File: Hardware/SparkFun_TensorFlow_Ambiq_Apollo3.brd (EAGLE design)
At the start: 40 x 40 mm, 122 parts, among them J5 CORTEX_DEBUG_PTH, J6 CAMERA-0V7670, M1 MEMS_MICROPHONESPW2430HR5H-B, M2 MEMS_MICROPHONESPW2430HR5H-B, U1 AMBIQ-APOLLO3KBR, U2 LIS2DH12, U3 1.8V, U4 LMV358, Y1 32MHz, Y2 32.768kHz

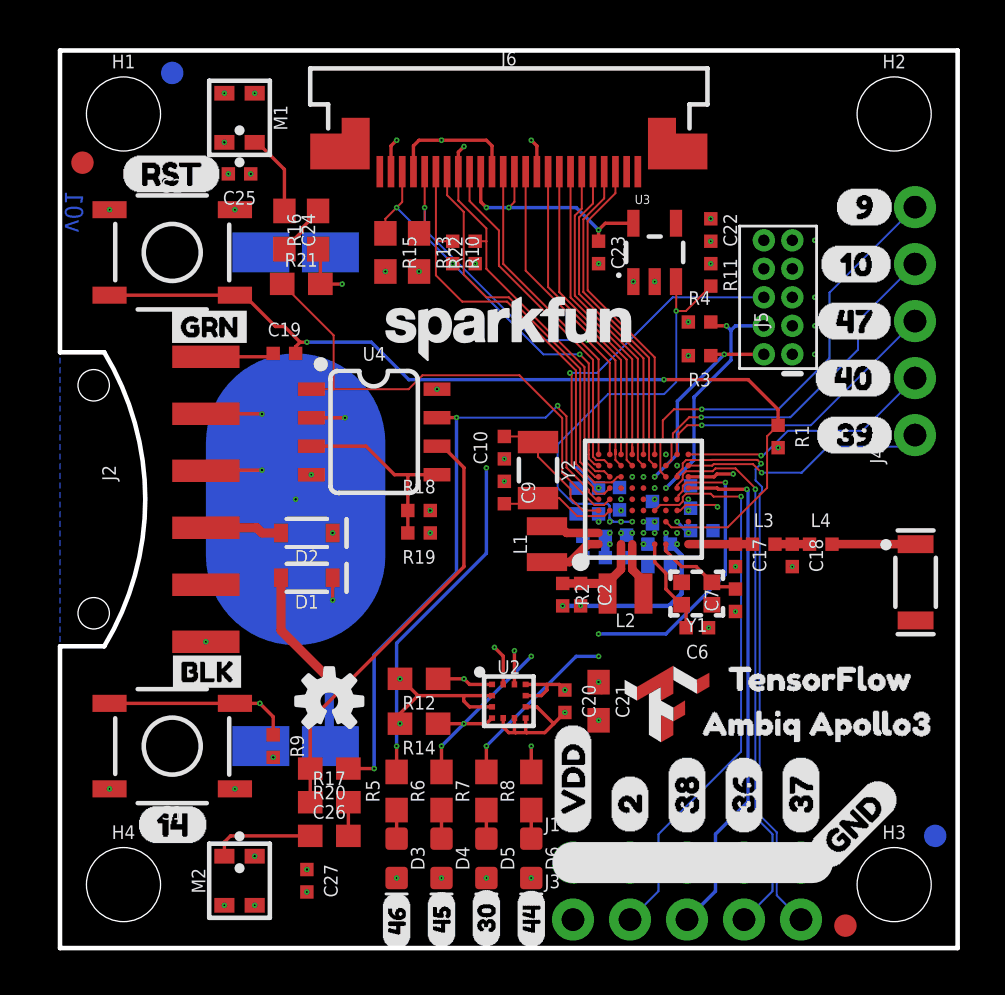
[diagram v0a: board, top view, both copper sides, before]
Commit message: Setting trace width/clearance to 5mil, via size to .2mm min
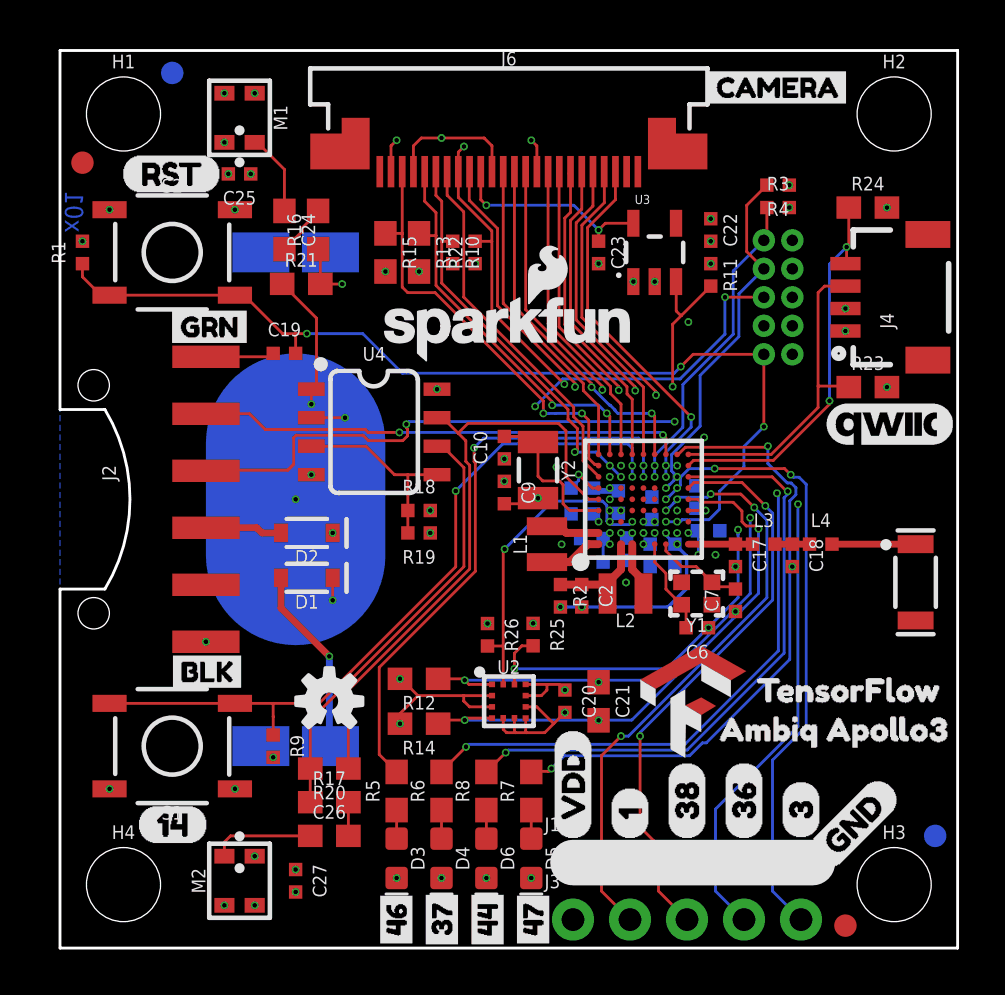
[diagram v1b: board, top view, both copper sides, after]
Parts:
- removed U$1: (no value), tensorflow#t#2#png:TENSORFLOW#T#2#PNG
- removed U$22, U$32: (no value), buzzard_labels:478
- removed U$23, U$33: (no value), buzzard_labels:109
- removed U$24: (no value), buzzard_labels:910
- removed U$25: (no value), buzzard_labels:4420
- removed U$31: (no value), buzzard_labels:407
- added R23, R24: 4.7k, SparkFun-Resistors:0603
- added R25, R26: 10k, ambiq:0402-TIGHT
- J4: device SparkFun-Connectors:1X05_NO_SILK -> SparkFun-Connectors:1X04_1MM_RA
- LOGO1: value SFE_LOGO_NAME.1_INCH -> SFE_LOGO_NAME_FLAME.1_INCH; device SparkFun-Aesthetics:SFE_LOGO_NAME_.1 -> SparkFun-Aesthetics:SFE_LOGO_NAME_FLAME_.1
- U$10: device buzzard_labels:22 -> buzzard_labels:31
- U$13: device buzzard_labels:375 -> buzzard_labels:31
- U$15: device buzzard_labels:396 -> buzzard_labels:461
- U$16: device buzzard_labels:4617 -> buzzard_labels:372
- U$17: device buzzard_labels:4519 -> buzzard_labels:443
- U$18: device buzzard_labels:3018 -> buzzard_labels:470
- U$19: device buzzard_labels:910 -> Labels:QWIIC_COPYRIGHT_SMALL
- U$20: device buzzard_labels:396 -> buzzard_labels:CAMERA3
- U$21: device buzzard_labels:407 -> tensorflow#t#2#png-5mm:TENSORFLOW#T#2#PNG
- U$5: device buzzard_labels:22 -> buzzard_labels:10
- U$8: device buzzard_labels:375 -> buzzard_labels:10
- moved R1 32.1 mm to (1.00, 31.0), turned to 90 degrees
- moved U$15 29.6 mm to (15.0, -0.25), turned to 90 degrees
- moved U$20 17.9 mm to (28.4, 38.4), flipped to the top
- moved U$21 17.1 mm to (28.2, 11.0), flipped to the top
- moved U$19 9.95 mm to (37.0, 23.4)
- moved U$10 7.62 mm to (33.0, 4.83)
- moved U$8 7.62 mm to (25.4, 4.83), flipped to the bottom
- moved R3 7.47 mm to (32.0, 33.0), turned to 0 degrees
- moved R4 7.03 mm to (32.0, 34.0), turned to 180 degrees
- moved J4 6.88 mm to (35.0, 29.0)
- moved U$18 2.10 mm to (21.1, -0.25)
- moved U$17 2.07 mm to (19.1, -0.25)
- moved U$16 2.02 mm to (17.0, -0.25)
- moved D5 2.00 mm to (21.0, 4.00)
- moved D6 2.00 mm to (19.0, 4.00)
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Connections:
- removed net !RST: J5.10
- removed net GPIO0/CAM_XCLK: J6.13, U1.H4
- removed net GPIO10_J4_4: J4.4, U1.G8
- removed net GPIO17/CAMERA_DVDD_EN: R11.2, U1.D3, U3.3
- removed net GPIO18/ACCEL_INT1: U1.C5, U2.12
- removed net GPIO19/ACCEL_INT2: U1.C3, U2.11
- removed net GPIO2_J3_2: J3.2, U1.F4
- removed net GPIO30/LED_YELLOW: R7.2, U1.F6
- removed net GPIO37_J3_5: J3.5, U1.H7
- removed net GPIO39_J4_1: J4.1, U1.J8
- removed net GPIO40_J4_2: J4.2, U1.J9
- removed net GPIO45/LED_BLUE: R6.2, U1.F5
- removed net GPIO47_J4_3: J4.3, U1.H9
- removed net GPIO7/CAMERA_Y2: J6.22, U1.F9
- removed net GPIO9_J4_5: J4.5, U1.G7
- new net GPIO0/ACCEL_INT2: R25.2, U1.H4, U2.11
- new net GPIO10/CAMERA_DVDD_EN: R11.2, U1.G8, U3.3
- new net GPIO17/ACCEL_INT1: R26.2, U1.D3, U2.12
- new net GPIO1_J3_2: J3.2, U1.G4
- new net GPIO37_LED_BLUE: R6.2, U1.H7
- new net GPIO39_QWIIC_SCK: J4.4, R24.1, U1.J8
- new net GPIO3_J3_5: J3.5, U1.G5
- new net GPIO40_QWIIC_SDA: J4.3, R23.1, U1.J9
- new net GPIO47/LED_YELLOW: R7.2, U1.H9
- new net GPIO7/CAM_XCLK: J6.13, U1.F9
- new net GPIO9/CAMERA_Y2: J6.22, U1.G7
- net AMBIQ_!RST: now also J5.10
- net GND: now also J4.1
- net VDD: now also J4.2, R23.2, R24.2, R25.1, R26.1
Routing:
- net GPIO37_LED_BLUE: track 0.00 -> 29.1 mm, vias 0 -> 3
- net GPIO47/LED_YELLOW: track 0.00 -> 28.0 mm, vias 0 -> 2
- net GPIO3_J3_5: track 0.00 -> 27.9 mm, vias 0 -> 3
- net GPIO1_J3_2: track 0.00 -> 26.9 mm, vias 0 -> 4
- net GPIO37_J3_5: track 25.7 -> 0.00 mm, vias 1 -> 0
- net GPIO2_J3_2: track 25.2 -> 0.00 mm, vias 1 -> 0
- net GPIO0/CAM_XCLK: track 21.4 -> 0.00 mm, vias 2 -> 0
- net GPIO0/ACCEL_INT2: track 0.00 -> 20.0 mm, vias 0 -> 3
- net GPIO9_J4_5: track 19.5 -> 0.00 mm, vias 1 -> 0
- net GPIO17/CAMERA_DVDD_EN: track 19.2 -> 0.00 mm, vias 2 -> 0
- net GPIO39_QWIIC_SCK: track 0.00 -> 17.3 mm, vias 0 -> 2
- net GPIO30/LED_YELLOW: track 16.6 -> 0.00 mm, vias 3 -> 0
- net GPIO45/LED_BLUE: track 16.6 -> 0.00 mm, vias 3 -> 0
- net GPIO9/CAMERA_Y2: track 0.00 -> 16.5 mm, vias 0 -> 2
- net GPIO10_J4_4: track 16.2 -> 0.00 mm, vias 1 -> 0
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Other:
- outline, holes or cut-outs redrawn
- board text added: "x01"
- board text removed: "v01"

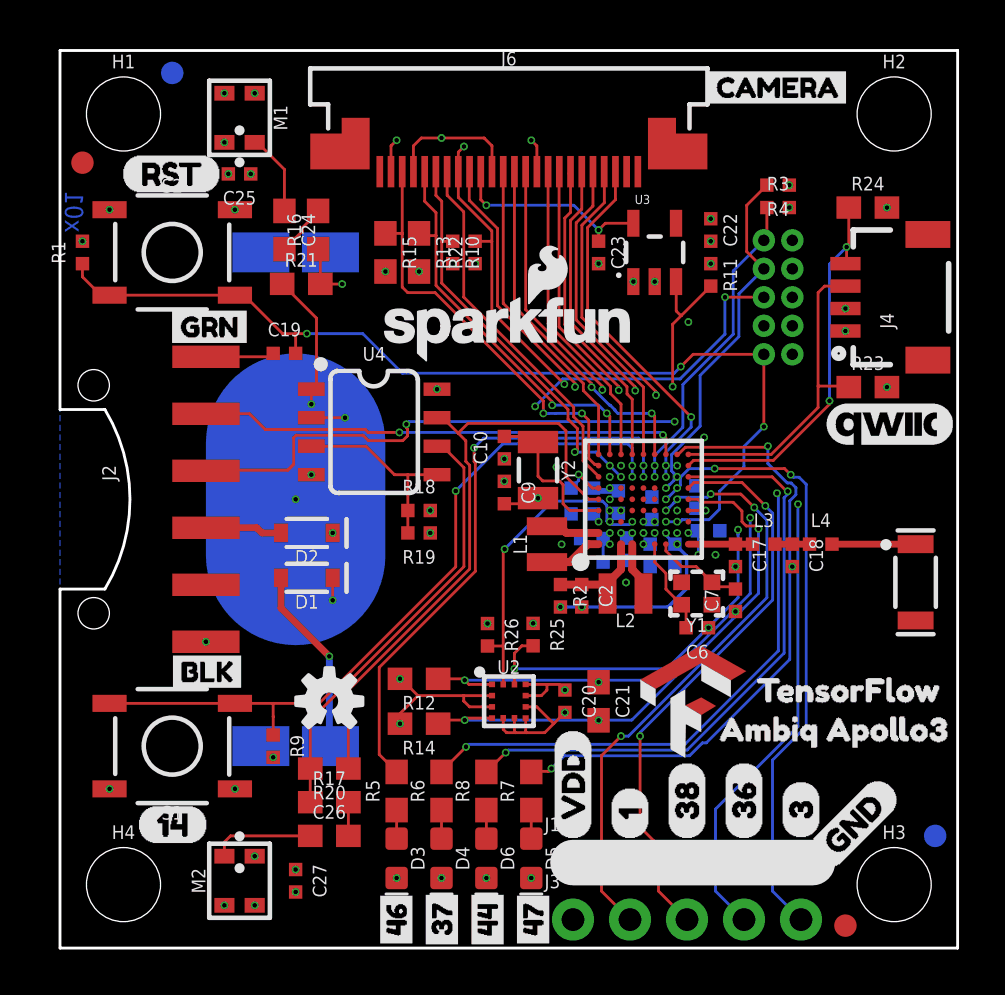
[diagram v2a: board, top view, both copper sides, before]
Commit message: Adding v01 of Tensorflow
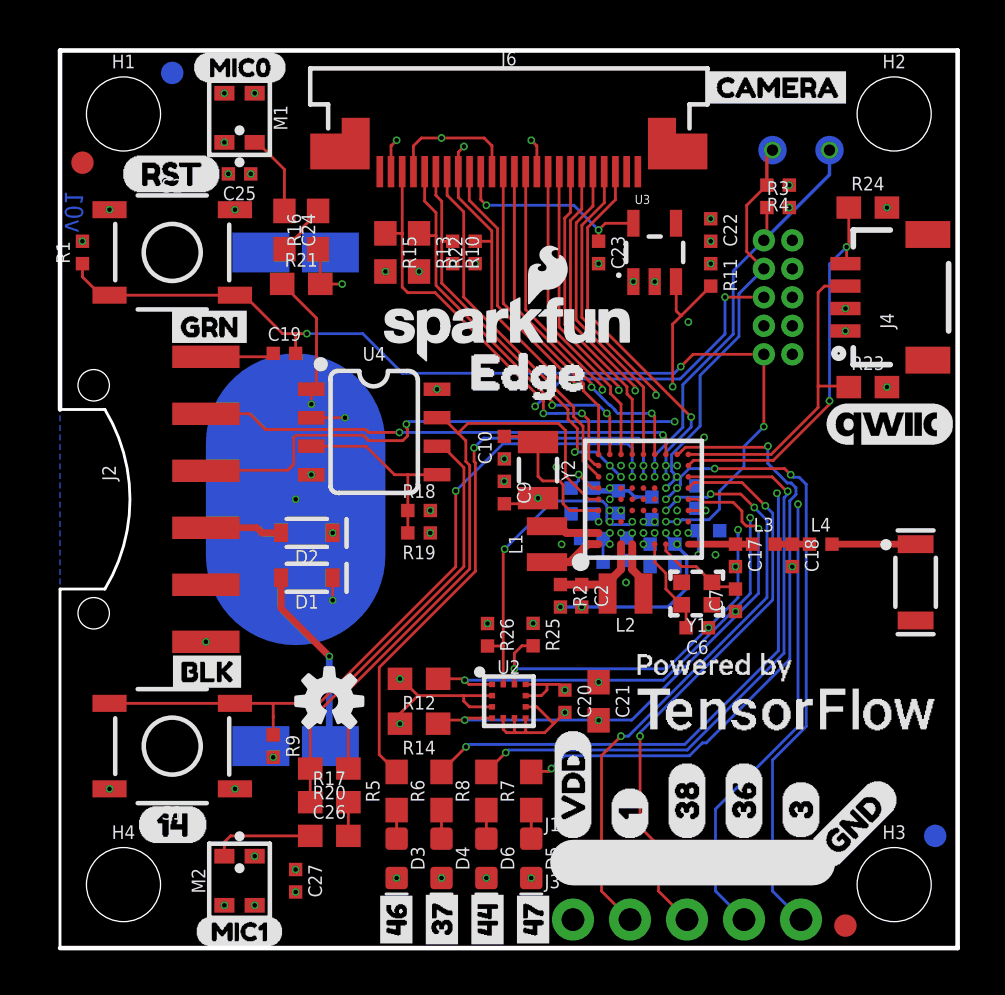
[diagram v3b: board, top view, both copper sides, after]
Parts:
- removed U$29: (no value), buzzard_labels:AMBIQ_APOLLO30
- removed U$30: (no value), buzzard_labels:TENSORFLOW1
- added TP1, TP2: TEST-POINT3X5, SparkFun-Connectors:PAD.03X.05
- added U$1: (no value), buzzard_labels:MIC00
- added U$22: (no value), buzzard_labels:MIC11
- added U$24: (no value), buzzard_labels:EDGE0
- M1, M2: value MEMS_MICROPHONESPW2430HR5H-B -> MEMS_MIC
- U$21: device tensorflow#t#2#png-5mm:TENSORFLOW#T#2#PNG -> PoweredBy_TF#jpg:POWEREDBY_TF#JPG
- moved U$21 4.10 mm to (32.3, 11.7)
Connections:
- net GPIO20/SWDCK: now also TP1.P$1
- net GPIO21/SWDIO: now also TP2.P$1
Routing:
- net GPIO21/SWDIO: track 14.1 -> 19.3 mm, vias 1 -> 2
- net GPIO20/SWDCK: track 16.1 -> 17.8 mm, vias 1 -> 2
- net GND: track 11.0 -> 12.7 mm
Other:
- board text added: "Jim Lindblom"
- board text added: "This is a 4-layer board!"
- board text added: "v01"
- board text removed: "x01"

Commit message: Disconnecting DVDD from VDD, adding test points.
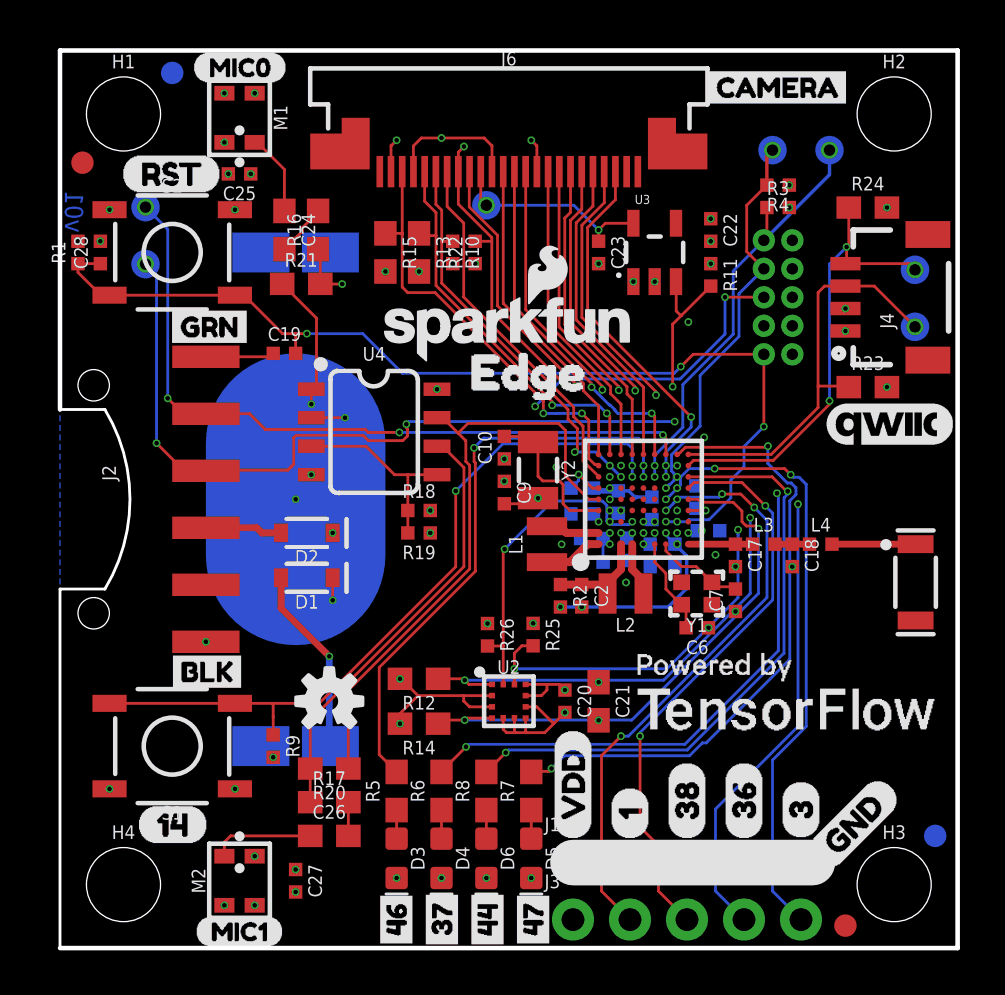
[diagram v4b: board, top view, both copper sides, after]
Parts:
- added C28: 0.1uF, ambiq:0402-TIGHT
- added TP3, TP4, TP5, TP6, TP7: TEST-POINT3X5, SparkFun-Connectors:PAD.03X.05
- moved R1 0.20 mm to (0.80, 31.0)
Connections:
- new net DVDD: C11.1, U1.H3
- net 1.8V: now also TP7.P$1
- net AMBIQ_!RST: now also C28.1
- net GND: now also C28.2
- net GPIO39_QWIIC_SCK: now also TP3.P$1
- net GPIO40_QWIIC_SDA: now also TP4.P$1
- net UART-RX/GPIO49: now also TP6.P$1
- net UART-TX/GPIO48: now also TP5.P$1
- net VDD: no longer C11.1, U1.H3
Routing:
- net UART-TX/GPIO48: track 21.7 -> 32.6 mm, vias 2 -> 4
- net UART-RX/GPIO49: track 25.1 -> 36.0 mm, vias 3 -> 5
- net GPIO40_QWIIC_SDA: track 14.9 -> 18.8 mm, vias 0 -> 1
- net GPIO39_QWIIC_SCK: track 17.3 -> 20.5 mm, vias 2 -> 3
- net VDD: track 24.7 -> 21.8 mm, vias 33 -> 31
- net DVDD: track 0.00 -> 1.47 mm, vias 0 -> 2
- net AMBIQ_!RST: track 44.3 -> 45.4 mm
- net GND: vias 50 -> 51

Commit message: Changes post-design review
- Silkscreen on back
- Add auto-reset diode
- Tuck battery overpaste in under connector
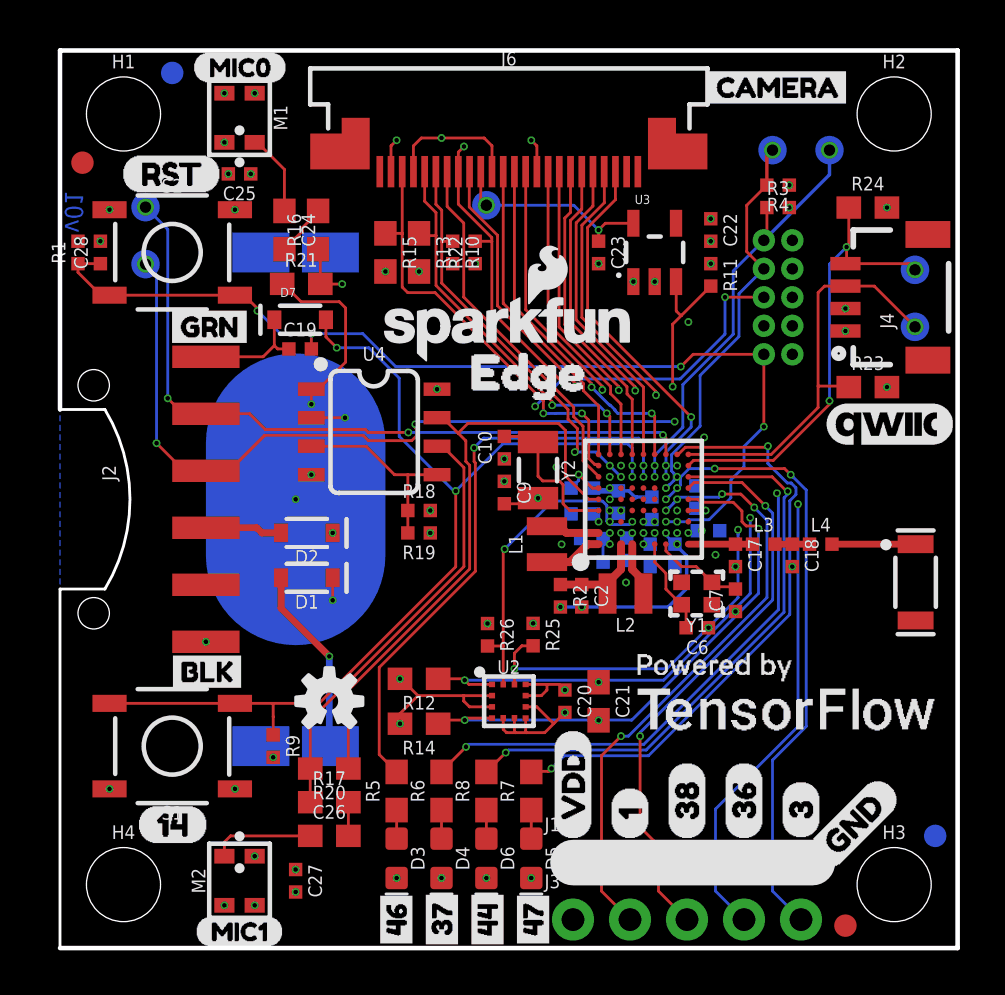
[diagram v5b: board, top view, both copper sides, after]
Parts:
- added D7: 250mA/100V, SparkFun-DiscreteSemi:SOD-323
- added U$23: (no value), buzzard_labels:EDGE0
- added U$25: (no value), PoweredBy_TF#jpg:POWEREDBY_TF#JPG
- added U$29: (no value), SparkFun-Aesthetics:SFE_LOGO_NAME_.1
- added U$30: (no value), SparkFun-Aesthetics:OSHW-LOGO-S
- BT1: device SparkFun-Batteries:BATTCON_20MM_4LEGS_OVERPASTE -> SparkFun-Batteries:BATTCON_20MM_4LEGS_OVERPASTE_INNER
- C28: value 0.1uF -> 1.0nF
- D1, D2: device SparkFun-DiscreteSemi:SOD-323 -> SparkFun-DiscreteSemi:SOD-323@1
- R18: value 10k -> 22k
- moved C19 0.73 mm to (10.7, 26.7)
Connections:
- removed net N$4: C19.1, J2.1
- new net DTR: C19.1, D7.C, J2.1
- net GPIO14/USER_BUTTON: now also D7.A
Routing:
- net GPIO14/USER_BUTTON: track 32.8 -> 43.7 mm, vias 2 -> 3
- net DTR: track 0.00 -> 5.12 mm
- net N$4: track 3.06 -> 0.00 mm
- net GPIO11/MIC0: track 21.1 -> 23.4 mm
- net GPIO47/LED_YELLOW: track 28.0 -> 26.9 mm
- net GPIO44/LED_GREEN: track 27.4 -> 26.4 mm
- net GPIO37_LED_BLUE: track 29.1 -> 28.0 mm
- net UART-RX/GPIO49: track 36.0 -> 35.3 mm
- net AMBIQ_!RST: track 45.4 -> 45.0 mm, vias 4 -> 5
